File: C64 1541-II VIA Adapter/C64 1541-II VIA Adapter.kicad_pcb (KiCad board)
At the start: 2 copper layers, 25.4 x 58.4 mm, 3 parts, among them J2 SpeedDOS, U1 6522

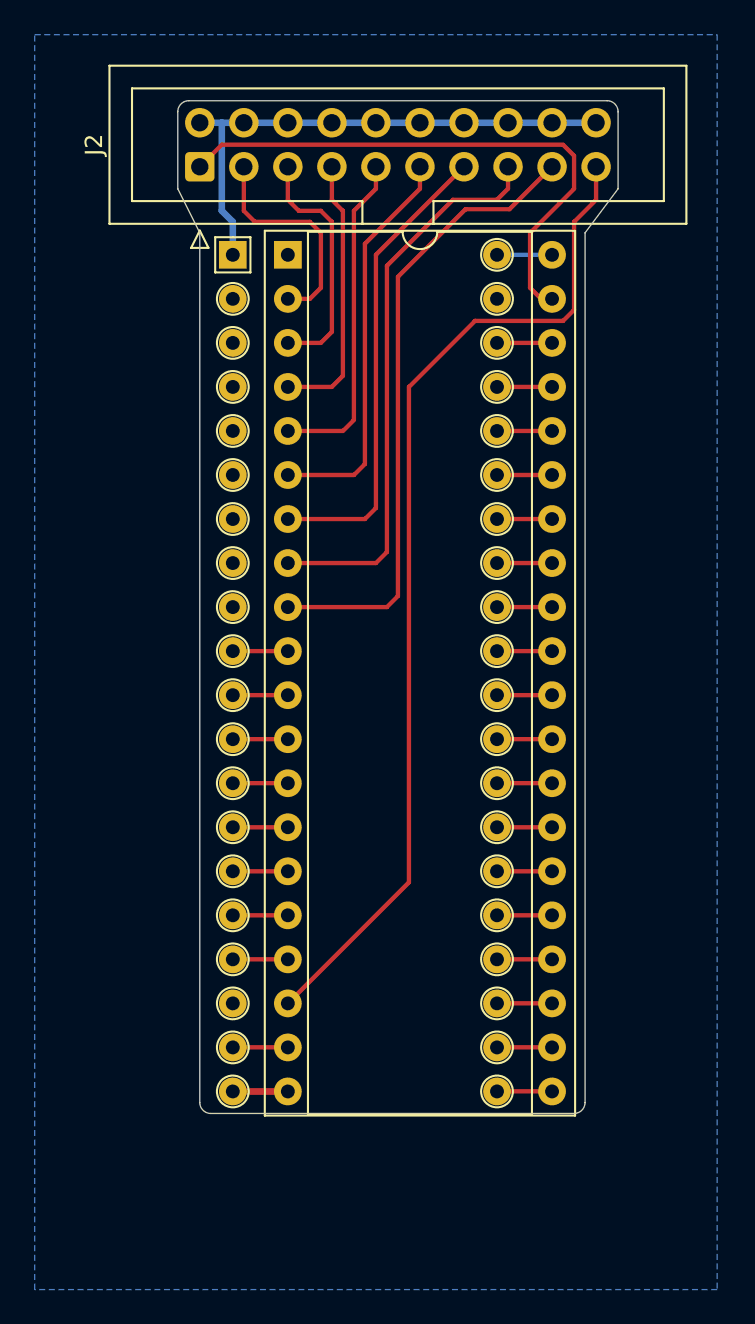
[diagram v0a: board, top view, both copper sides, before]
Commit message: User port adapter added
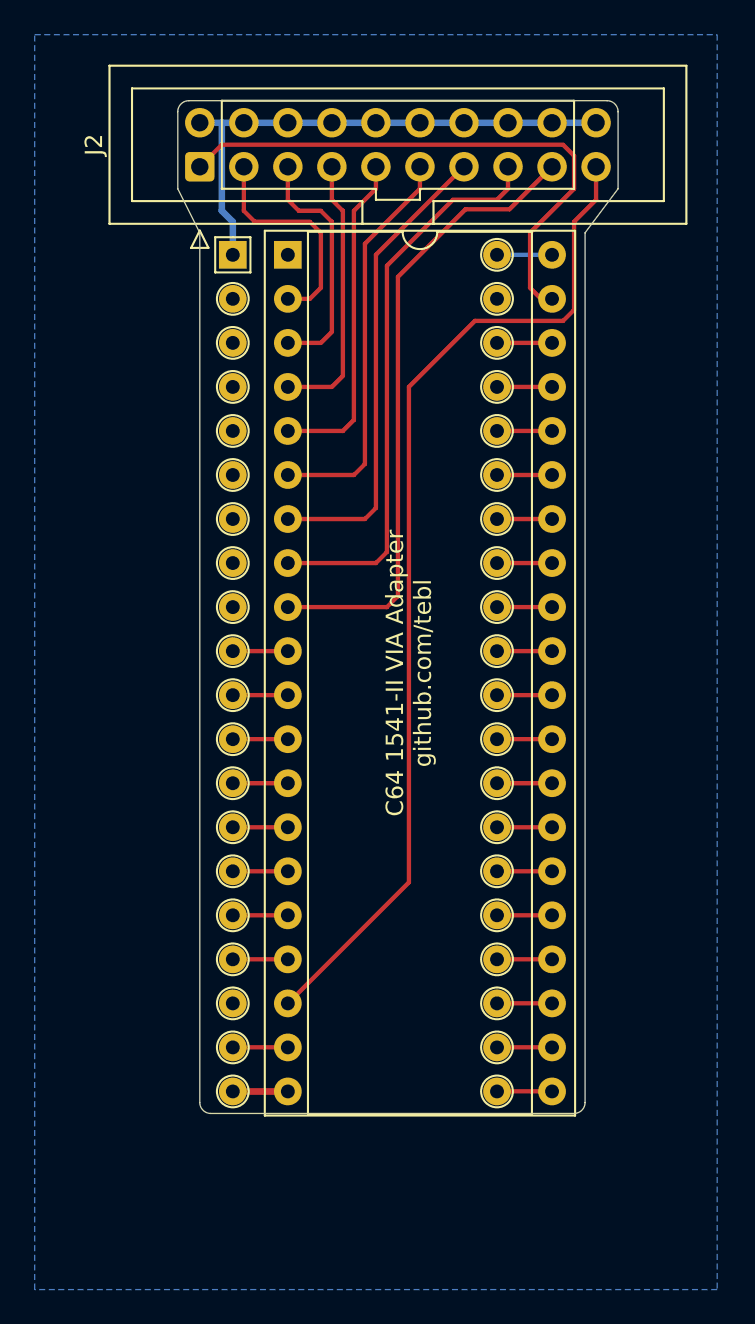
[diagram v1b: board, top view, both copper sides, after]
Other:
- board text added: "A1"
- board text added: "C64 1541-II VIA Adapter github.com/tebl"
- board text added: "Designed for use with C64 XUM1541, C64 XUM1541-II and C64 SpeedDOS Adapter (read documentation before use). Licensed under CERN OHL v1.2"
- board text added: "U1"

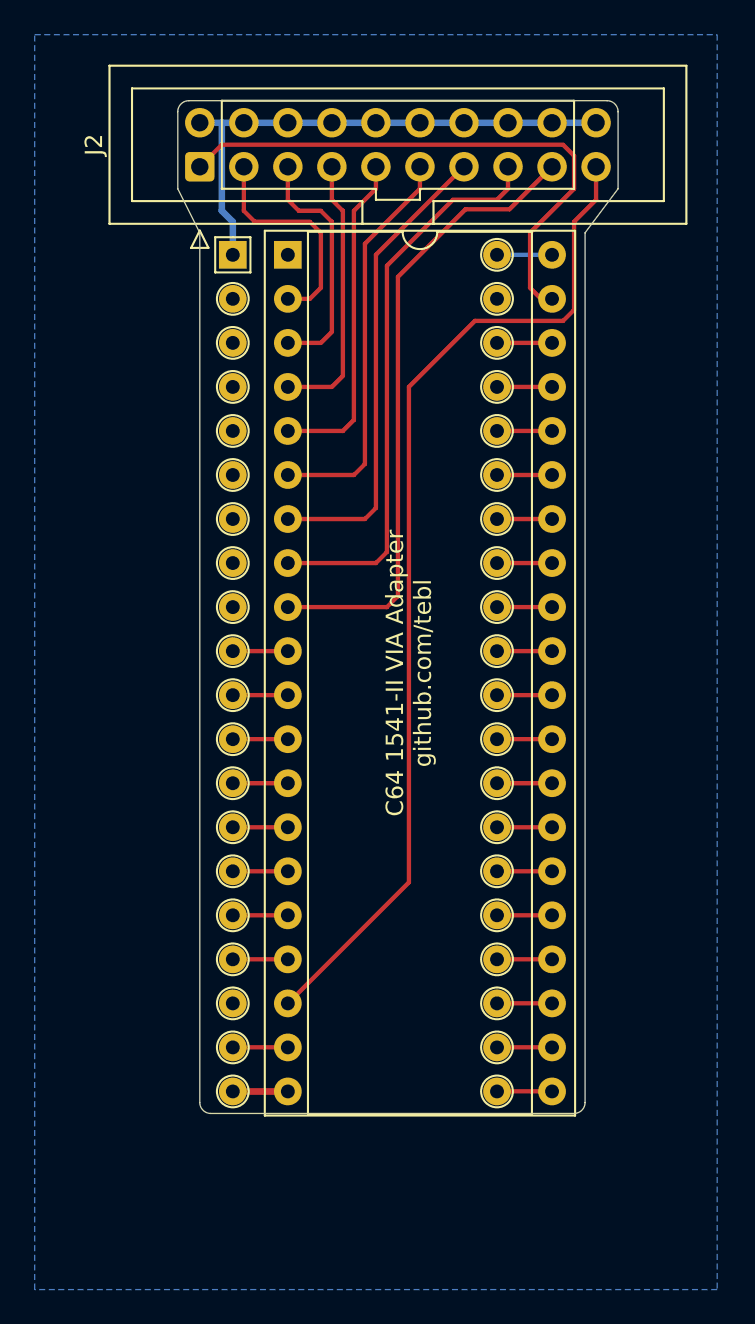
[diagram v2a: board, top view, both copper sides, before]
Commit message: Moved connector to clear stepper motor
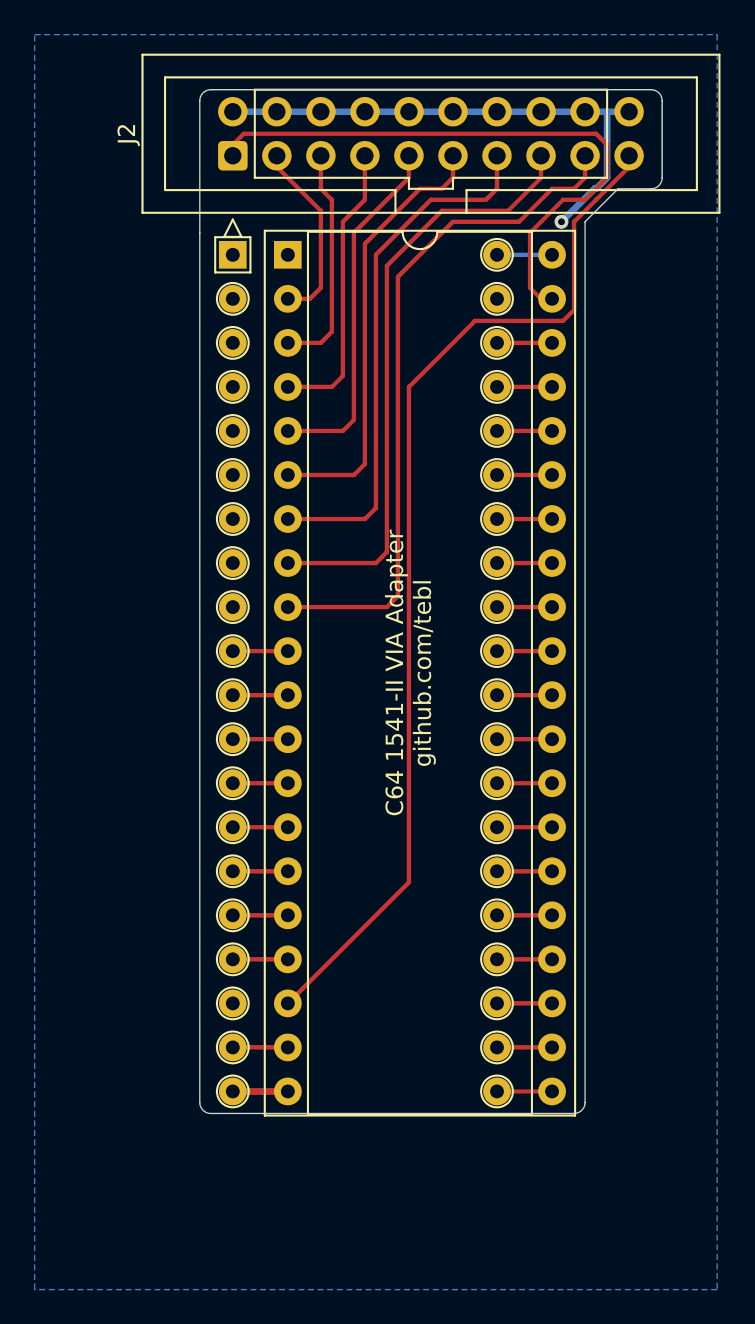
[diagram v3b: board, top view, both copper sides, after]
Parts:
- moved J2 2.01 mm to (102.2, 56.5)
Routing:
- net /PA7: track 36.5 -> 40.1 mm
- net /PA4: track 23.2 -> 26.0 mm
- net /PA6: track 32.6 -> 35.4 mm
- net /PA5: track 27.1 -> 29.8 mm
- net /PA0: track 12.9 -> 10.2 mm
- net /CA2: track 32.6 -> 35.1 mm
- net /PA3: track 19.2 -> 21.3 mm
- net /PA1: track 14.1 -> 13.2 mm
- net /CB1: track 58.6 -> 59.4 mm
- net GND: track 30.7 -> 30.4 mm, vias 0 -> 1
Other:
- board size 25.4 x 58.4 mm -> 26.7 x 59.1 mm

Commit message: Link remaining pins
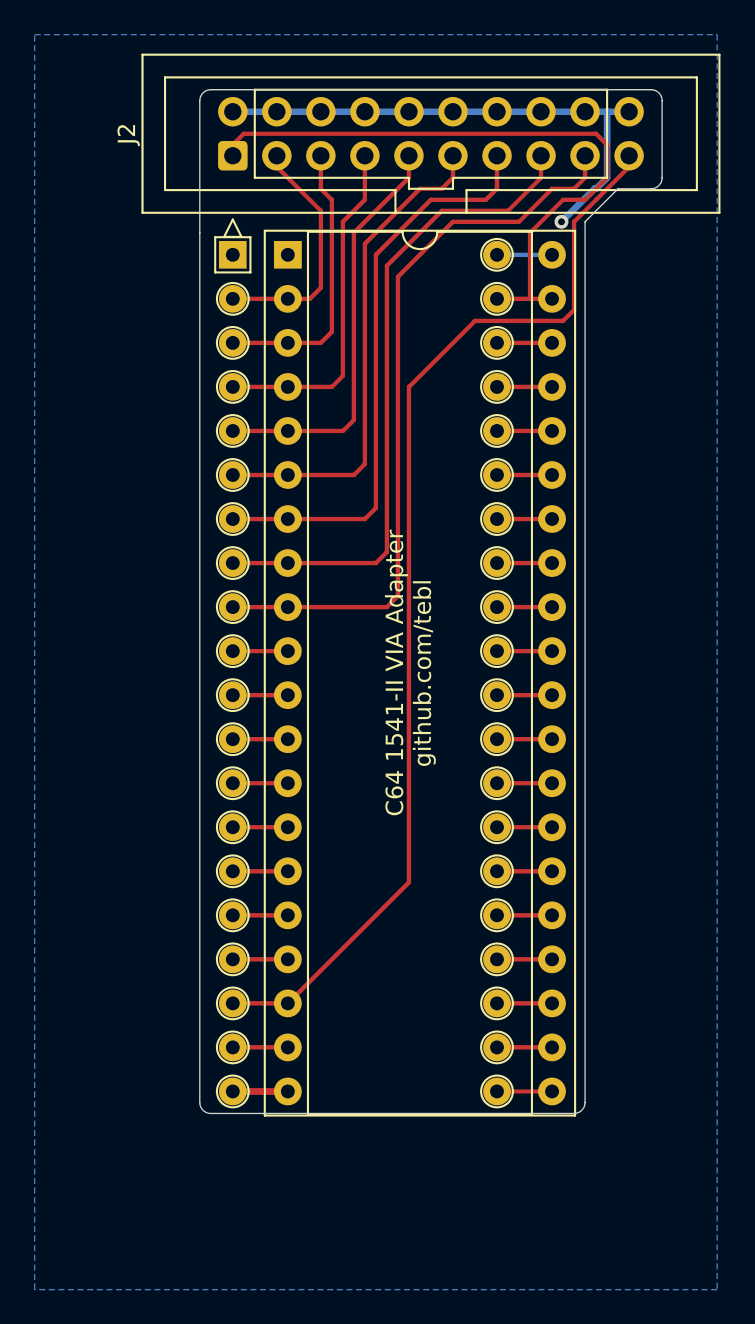
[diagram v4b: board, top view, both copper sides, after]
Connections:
- A1 pad 18: (no net) -> /CB1
- A1 pad 2: (no net) -> /PA0
- A1 pad 3: (no net) -> /PA1
- A1 pad 39: (no net) -> /CA2
- A1 pad 4: (no net) -> /PA2
- A1 pad 5: (no net) -> /PA3
- A1 pad 6: (no net) -> /PA4
- A1 pad 7: (no net) -> /PA5
- A1 pad 8: (no net) -> /PA6
- A1 pad 9: (no net) -> /PA7
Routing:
- net /PA1: track 13.2 -> 16.4 mm
- net /PA7: track 40.1 -> 43.3 mm
- net /PA6: track 35.4 -> 38.6 mm
- net /PA4: track 26.0 -> 29.1 mm
- net /PA3: track 21.3 -> 24.4 mm
- net /PA2: track 16.0 -> 19.2 mm
- net /PA0: track 10.2 -> 13.4 mm
- net /CB1: track 59.4 -> 62.6 mm
- net /PA5: track 29.8 -> 33.0 mm
- net /CA2: track 35.1 -> 37.4 mm

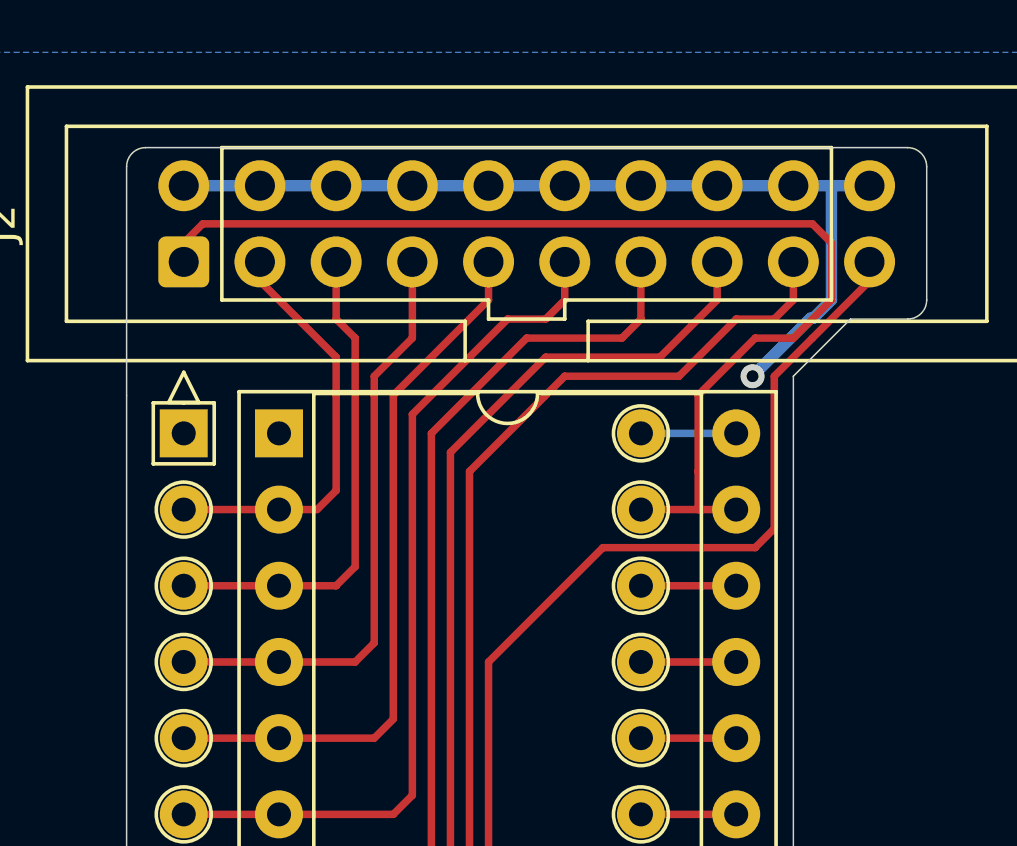
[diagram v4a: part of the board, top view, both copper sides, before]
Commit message: Added GND jumper
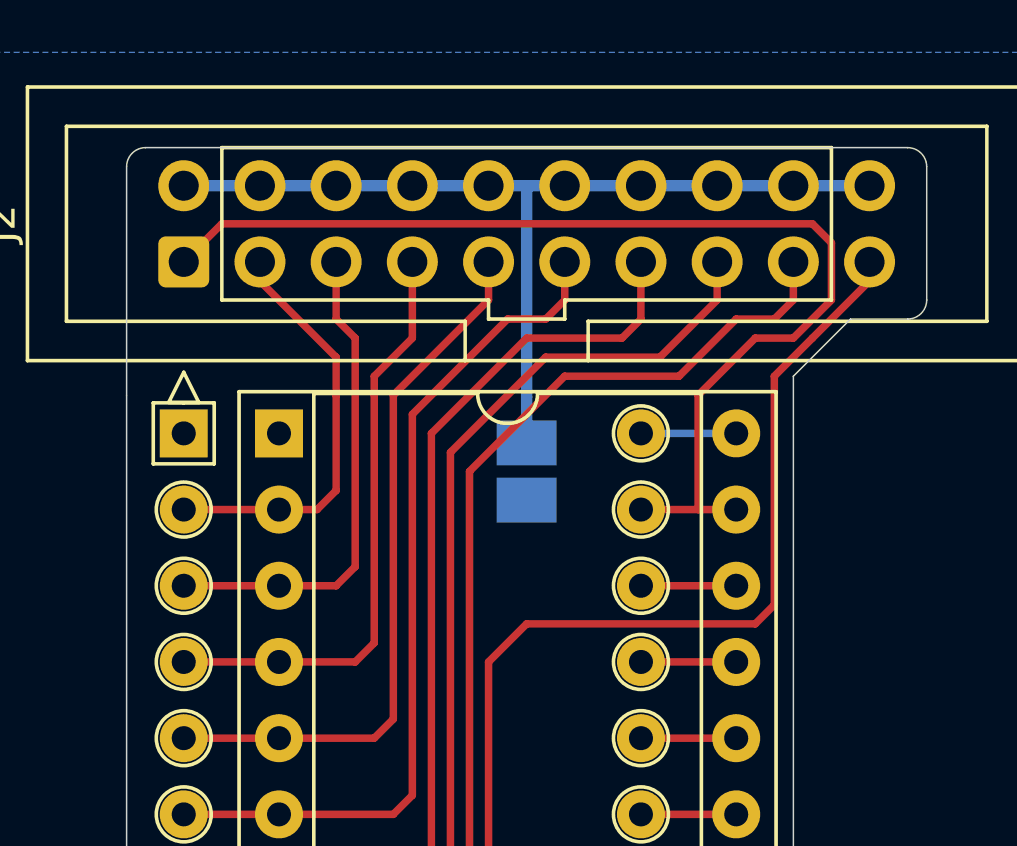
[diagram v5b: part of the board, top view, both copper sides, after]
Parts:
- added JP1: GND, solder_bridge:bridge_r, B.Cu at (113.7, 62.5)
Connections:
- J2 pad 11: GND -> Net-(J2-Pad11)
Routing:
- net Net-(J2-Pad11): track 0.00 -> 31.5 mm
- net GND: track 30.4 -> 0.00 mm, vias 1 -> 0
- net /CB1: track 62.6 -> 64.1 mm

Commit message: Gerber export
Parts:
- JP1: moved to F.Cu
- moved JP1 3.49 mm to (113.7, 66.0), turned to 0 degrees
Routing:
- net Net-(J2-Pad11): track 31.5 -> 35.0 mm, vias 0 -> 1
- net GND: track 0.00 -> 1.91 mm, vias 0 -> 1
